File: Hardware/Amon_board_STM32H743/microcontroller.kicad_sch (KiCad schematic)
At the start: 23 parts, among them J4 HAB-VCR-010-LF, U9 STM32H743VIT6, Y1 48MHz, Y2 32.768kHz

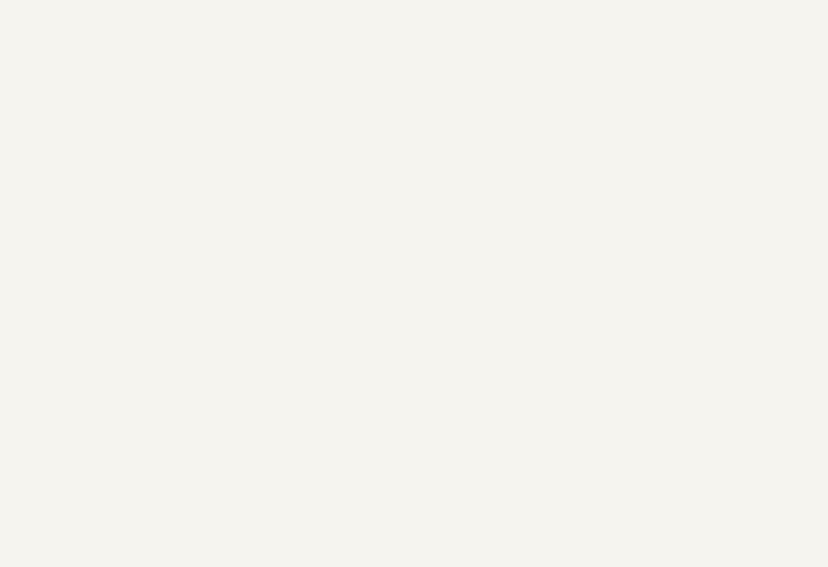
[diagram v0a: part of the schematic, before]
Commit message: Update
compas driver - untested
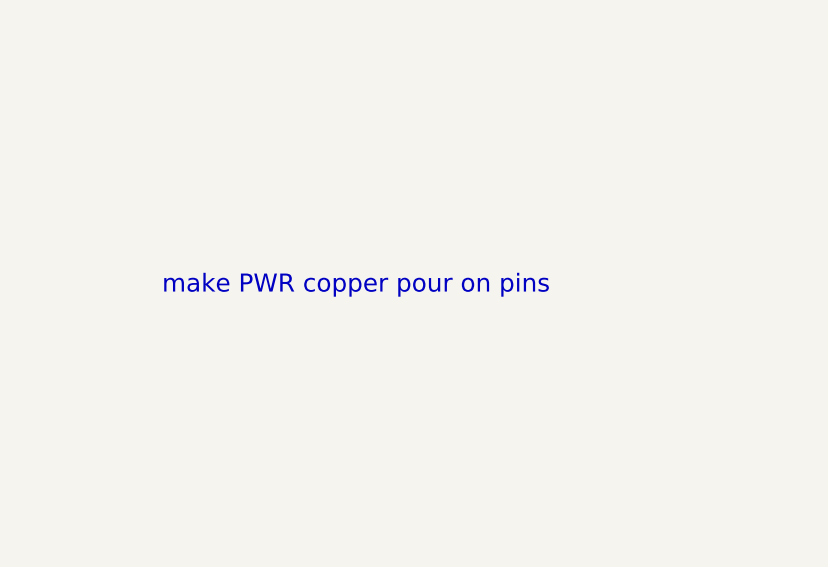
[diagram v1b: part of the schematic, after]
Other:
- note added: "make PWR copper pour on pins"
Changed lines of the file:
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@@
+		)
+	)
+	(text "make PWR copper pour on pins"
+		(exclude_from_sim no)
+		(at 143.002 146.558 0)
+		(effects
+			(font
+				(size 2 2)
+				(color 255 3 60 1)
+			)
+			(justify left bottom)
 		)
 	)

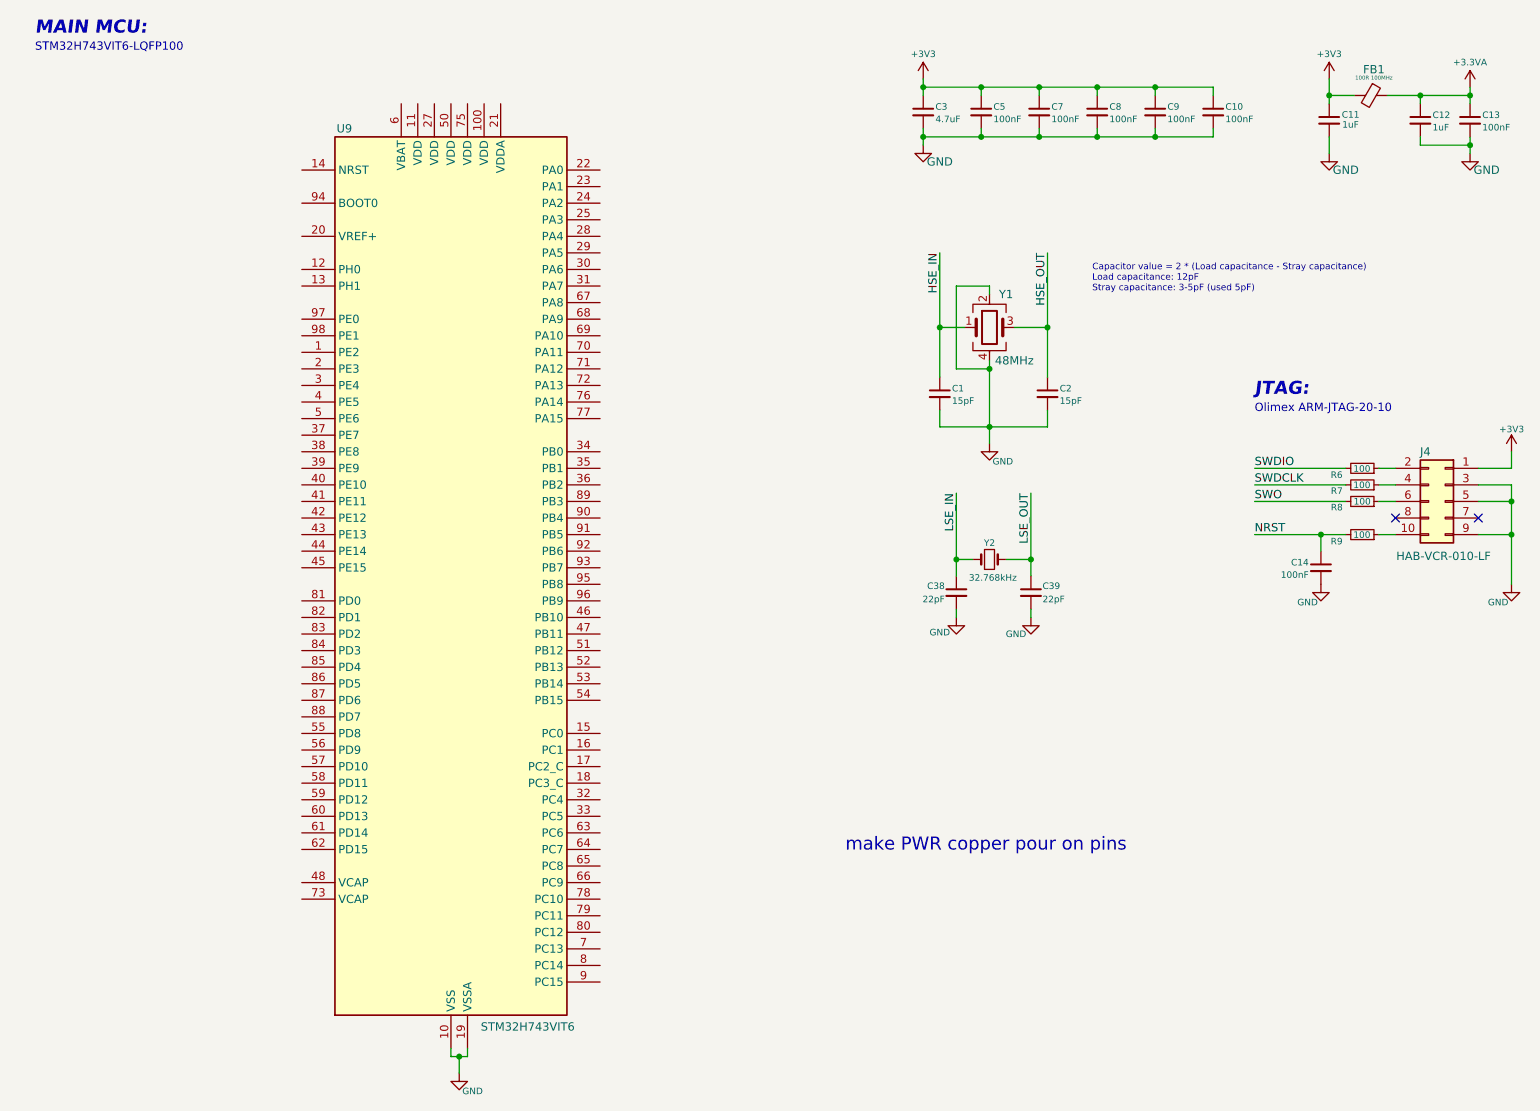
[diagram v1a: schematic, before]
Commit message: Update
added first flight path buffer
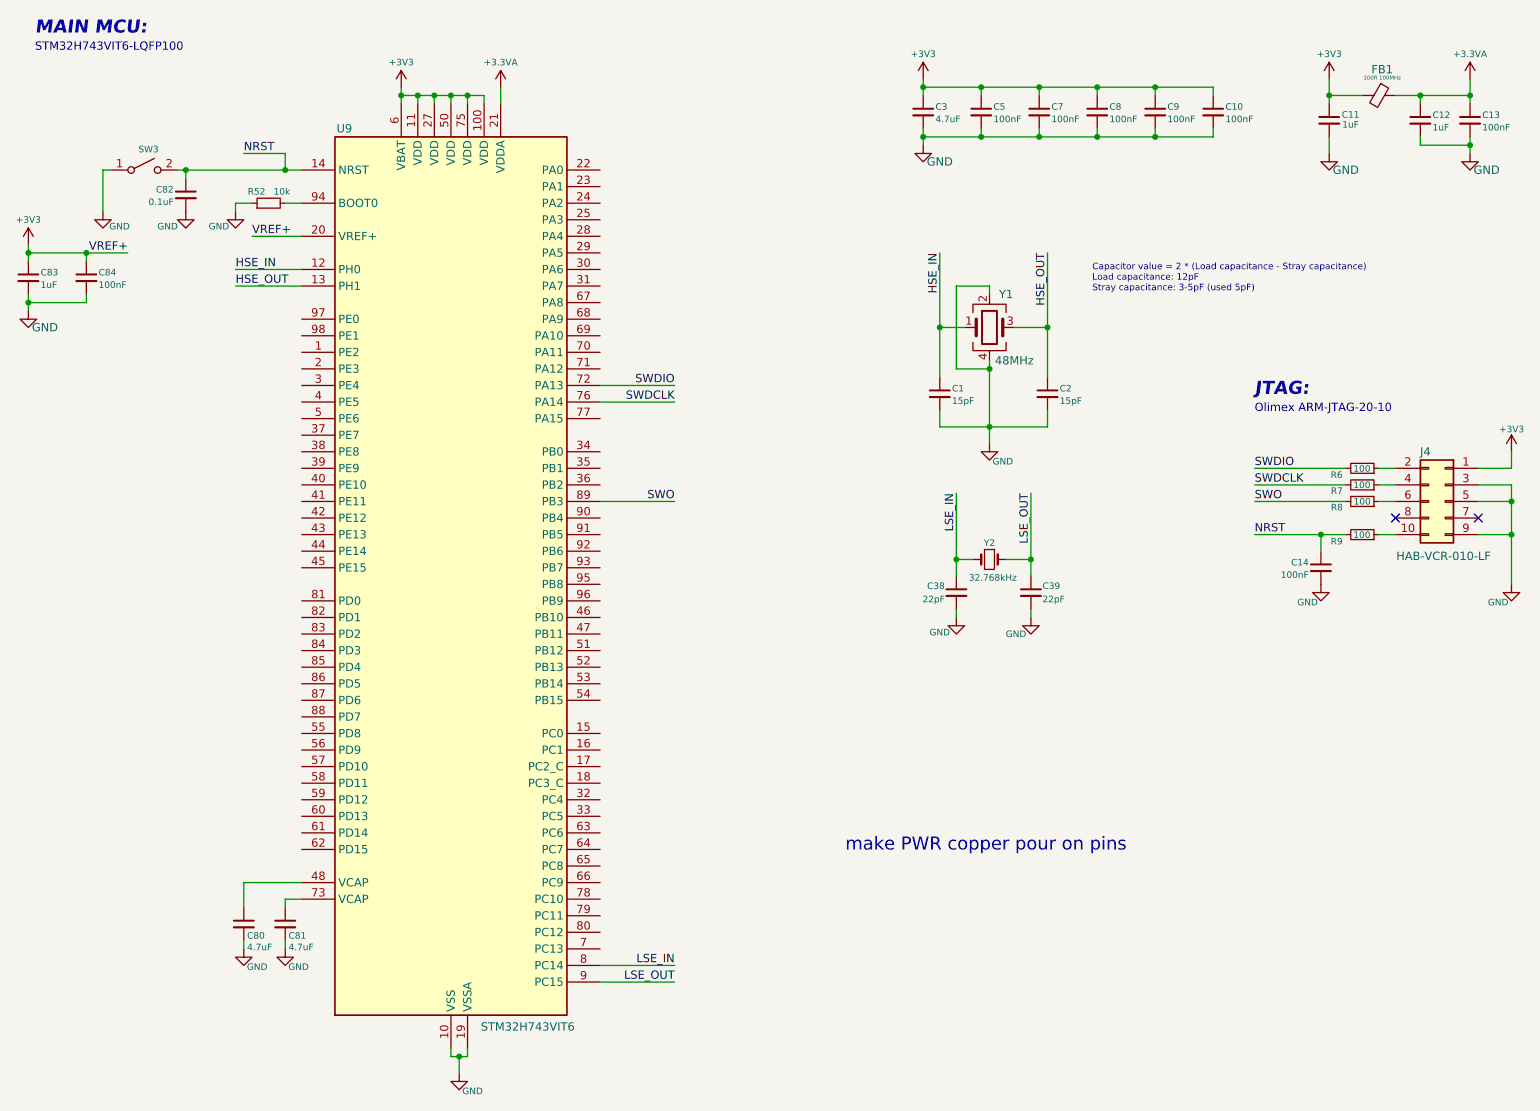
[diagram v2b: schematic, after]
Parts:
- added C80, C81: 4.7uF, Capacitor_SMD:C_0402_1005Metric, symbol Device:C_Small
- added C82: 0.1uF, Capacitor_SMD:C_0603_1608Metric, symbol Device:C_Small
- added C83: 1uF, Capacitor_SMD:C_0603_1608Metric, symbol Device:C_Small
- added C84: 100nF, Capacitor_SMD:C_0603_1608Metric, symbol Device:C_Small
- added R52: 10k, Resistor_SMD:R_0603_1608Metric, symbol Device:R_Small
- added SW3: SW_SPST, Button_Switch_SMD:SW_Push_1P1T_NO_CK_KMR2, symbol Switch:SW_SPST
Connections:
- net +3.3VA: now also U9.21 (VDDA)
- net +3V3: now also U9.100 (VDD), U9.11 (VDD), U9.20 (VREF+), U9.27 (VDD), U9.50 (VDD), U9.6 (VBAT), U9.75 (VDD), C83.1, C84.1
- net GND: now also C80.2, C81.2, C82.2, C83.2, C84.2, R52.1, SW3.1 (A)
- net HSE_IN: now also U9.12 (PH0)
- net HSE_OUT: now also U9.13 (PH1)
- net LSE_IN: now also U9.8 (PC14)
- net LSE_OUT: now also U9.9 (PC15)
- net NRST: now also U9.14 (NRST), C82.1, SW3.2 (B)
- net SWDCLK: now also U9.76 (PA14)
- net SWDIO: now also U9.72 (PA13)
- net SWO: now also U9.89 (PB3)
- net at U9.48 (VCAP): now also C80.1
- net at U9.73 (VCAP): now also C81.1
- net at U9.94 (BOOT0): now also R52.2
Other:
- moved on the sheet: FB1
